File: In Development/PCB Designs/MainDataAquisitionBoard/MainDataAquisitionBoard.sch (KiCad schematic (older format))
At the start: 19 parts, among them J1 Conn_01x08, J10 3v3, J11 TopR, J12 TopL, J13 BottomR, J14 BottomL, J15 RTC, J2 Conn_01x08, J3 GND, J4 1x24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

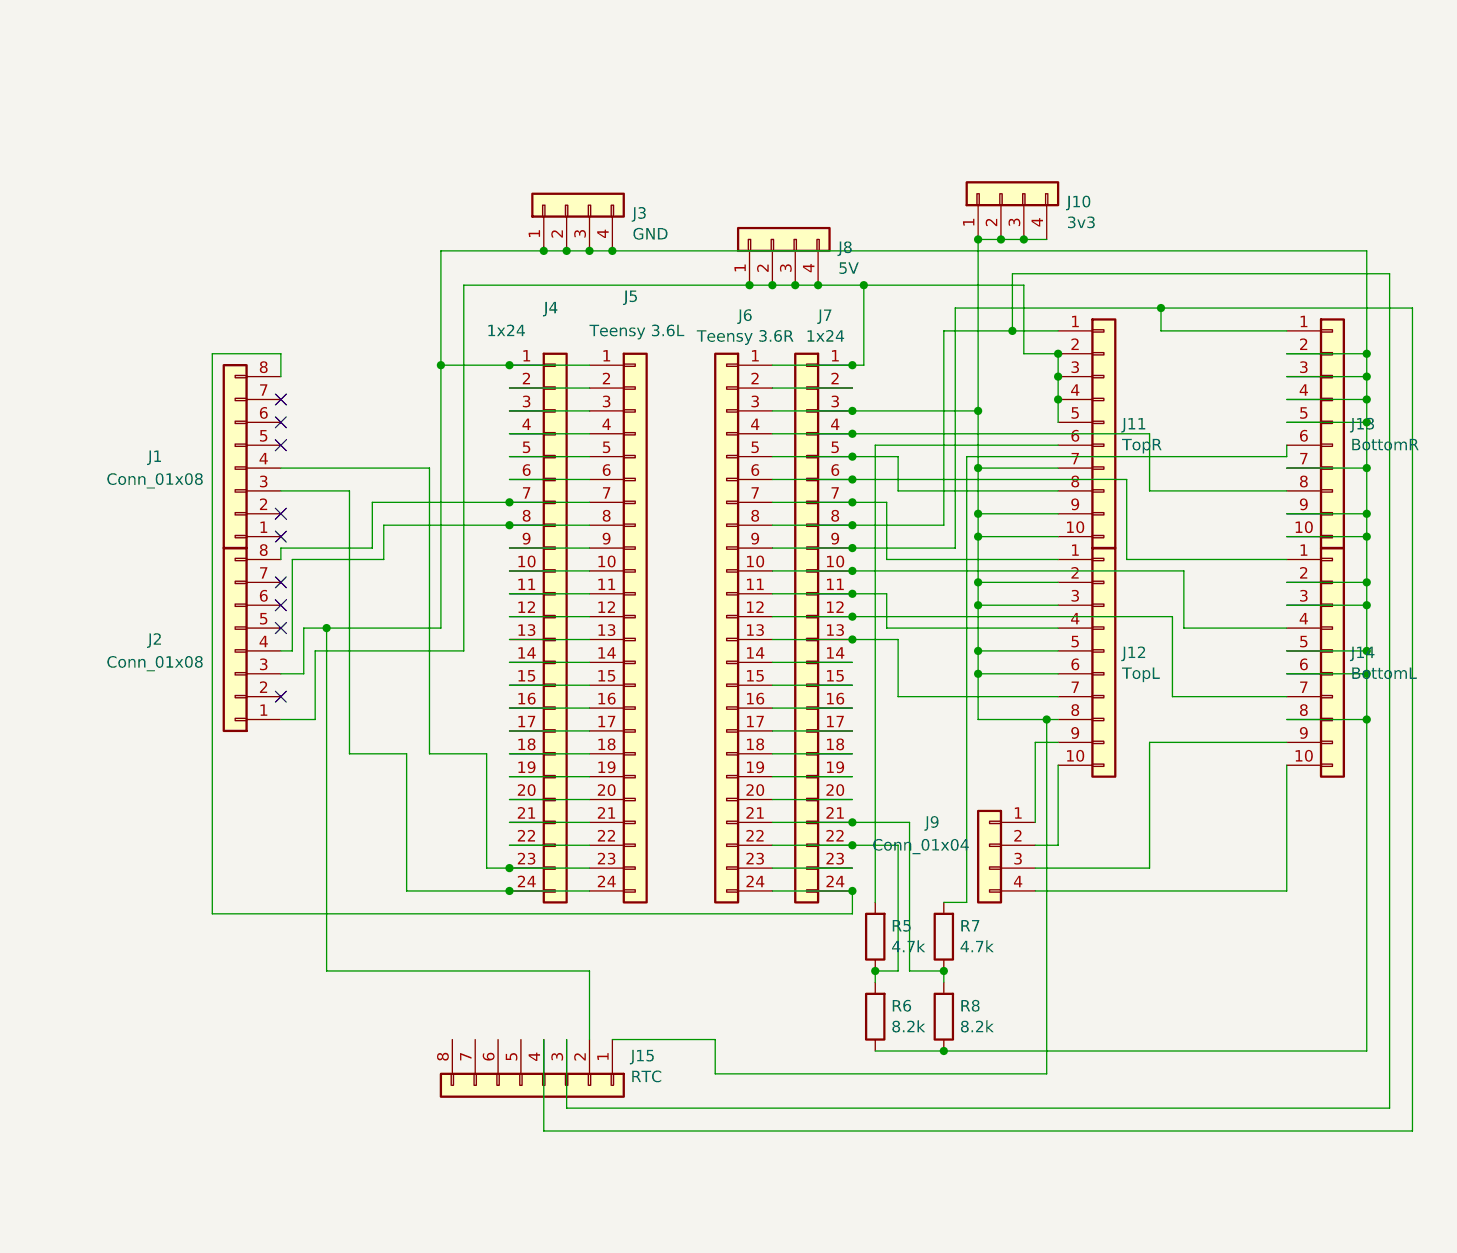
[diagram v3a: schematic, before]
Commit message: Finished Main DAQ PCB and eCVT controller PCB for design review
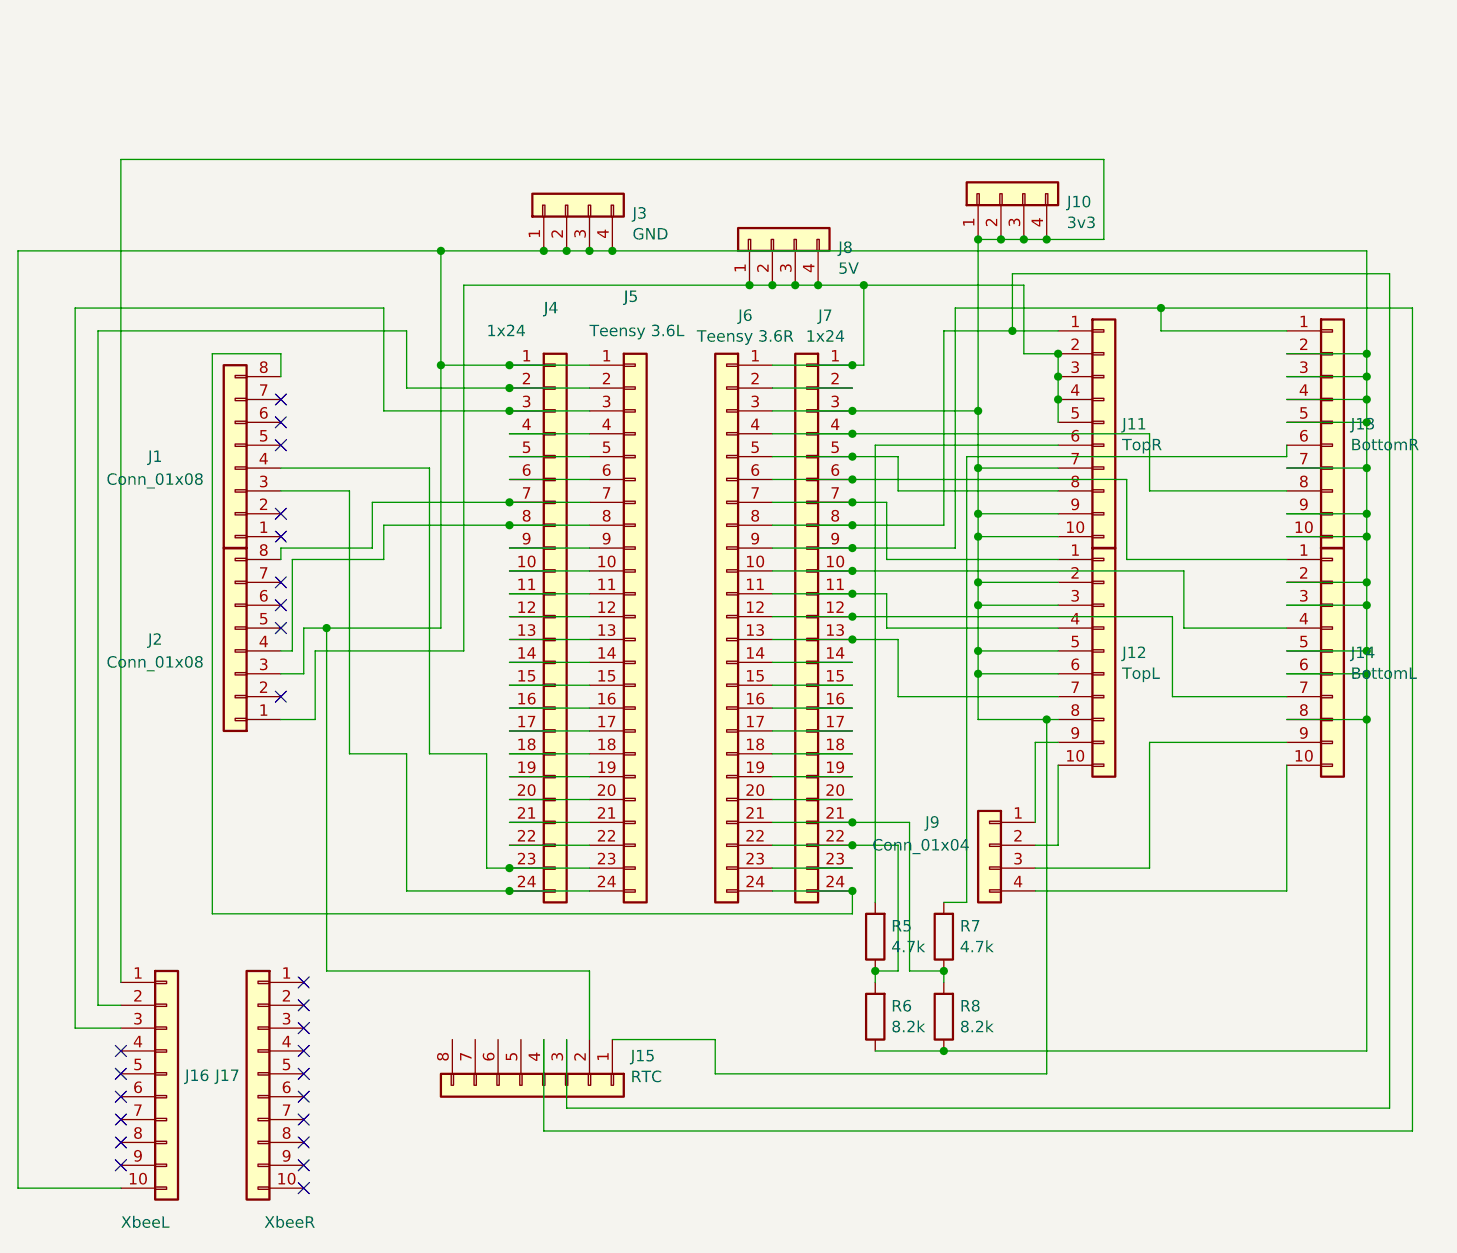
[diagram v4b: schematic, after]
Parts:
- added J16: XbeeL, Connector_PinHeader_2.54mm:PinHeader_1x10_P2.54mm_Vertical, symbol Connector_Generic:Conn_01x10
- added J17: XbeeR, Connector_PinHeader_2.54mm:PinHeader_1x10_P2.54mm_Vertical, symbol Connector_Generic:Conn_01x10
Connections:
- net at J13.10 (Pin_10), J13.2 (Pin_2), J13.3 (Pin_3)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: now also J16.10 (Pin_10)
- net at J4.2 (Pin_2), J5.2 (Pin_2): now also J16.2 (Pin_2)
- net at J4.3 (Pin_3), J5.3 (Pin_3): now also J16.3 (Pin_3)
- net at J10.1 (Pin_1), J10.2 (Pin_2), J10.3 (Pin_3)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: now also J16.1 (Pin_1)
- no-connect marks 9 -> 25
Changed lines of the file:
@@
 	4450 3050 4800 3050
-Wire Wire Line
-	4450 3150 4800 3150
 Wire Wire Line
 	4450 3250 4800 3250
@@
 Wire Wire Line
 	3650 4100 3650 5600
+$Comp
+L Connector_Generic:Conn_01x10 J16
+U 1 1 5E2846AA
+P 2950 6050
+F 0 "J16" H 3030 6042 50  0000 L CNN
+F 1 "XbeeL" H 2750 5400 50  0000 L CNN
+F 2 "Connector_PinHeader_2.54mm:PinHeader_1x10_P2.54mm_Vertical" H 2950 6050 50  0001 C CNN
+F 3 "~" H 2950 6050 50  0001 C CNN
+	1    2950 6050
+	1    0    0    -1
+$EndComp
+NoConn ~ 3550 5650
+NoConn ~ 3550 5750
+NoConn ~ 3550 5850
+NoConn ~ 3550 5950
+NoConn ~ 3550 6050
+NoConn ~ 3550 6150
+NoConn ~ 3550 6250
+NoConn ~ 3550 6350
+NoConn ~ 3550 6450
+NoConn ~ 3550 6550
+NoConn ~ 2750 6450
+NoConn ~ 2750 6350
+NoConn ~ 2750 6250
+NoConn ~ 2750 6150
+NoConn ~ 2750 6050
+NoConn ~ 2750 5950
+Wire Wire Line
+	2750 6550 2300 6550
+Wire Wire Line
+	2300 6550 2300 2450
+Wire Wire Line
+	2300 2450 4150 2450
+Connection ~ 4150 2450
+$Comp
+L Connector_Generic:Conn_01x10 J17
+U 1 1 5E28781E
+P 3350 6050
+F 0 "J17" H 3430 6042 50  0000 L CNN
+F 1 "XbeeR" H 3100 5400 50  0000 L CNN
+F 2 "Connector_PinHeader_2.54mm:PinHeader_1x10_P2.54mm_Vertical" H 3350 6050 50  0001 C CNN
+F 3 "~" H 3350 6050 50  0001 C CNN
+	1    3350 6050
+	-1   0    0    -1
+$EndComp
+Wire Wire Line
+	2750 5650 2750 2050
+Wire Wire Line
+	2750 2050 7050 2050
+Wire Wire Line
+	7050 2050 7050 2400
+Wire Wire Line
+	7050 2400 6800 2400
+Connection ~ 6800 2400
+Wire Wire Line
+	2750 5750 2650 5750
+Wire Wire Line
+	2650 5750 2650 2800
+Wire Wire Line
+	2650 2800 4000 2800
+Wire Wire Line
+	4000 2800 4000 3050
+Wire Wire Line
+	4000 3050 4450 3050
+Connection ~ 4450 3050
+Wire Wire Line
+	2750 5850 2550 5850
+Wire Wire Line
+	2550 5850 2550 2700
+Wire Wire Line
+	2550 2700 3900 2700
+Wire Wire Line
+	3900 2700 3900 3150
+Wire Wire Line
+	3900 3150 4450 3150
+Connection ~ 4450 3150
+Wire Wire Line
+	4450 3150 4800 3150
 $EndSCHEMATC

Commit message: Finished DAQ board and ready for initial production
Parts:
- added J18: Conn_02x03_Counter_Clockwise, Connector_PinHeader_2.54mm:PinHeader_2x03_P2.54mm_Vertical, symbol Connector_Generic:Conn_02x03_Counter_Clockwise
- added J19: Power in, CustomKiCADLibrary:PinHeader_1x02_P5.08mm_Vertical, symbol Connector_Generic:Conn_01x02
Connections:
- net at J13.10 (Pin_10), J13.2 (Pin_2), J13.3 (Pin_3)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: now also J1.1 (Pin_1), J19.2 (Pin_2); no longer J2.3 (Pin_3)
- net at J4.11 (Pin_11), J5.11 (Pin_11): now also J2.3 (Pin_3)
- net at J4.12 (Pin_12), J5.12 (Pin_12): now also J2.1 (Pin_1)
- net at J11.2 (Pin_2), J11.3 (Pin_3), J11.4 (Pin_4)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: now also J18.1 (Pin_1), J19.1 (Pin_1); no longer J2.1 (Pin_1), J6.1 (Pin_1), J7.1 (Pin_1)
- new net: J18.3 (Pin_3), J6.1 (Pin_1), J7.1 (Pin_1)
- no-connect marks 25 -> 28
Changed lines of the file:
@@
 $EndComp
-Wire Wire Line
-	4250 4200 4250 2600
-Wire Wire Line
-	6000 2600 6000 2950
 Wire Wire Line
 	5600 2950 5950 2950
 Connection ~ 5950 2950
 Wire Wire Line
-	5950 2950 6000 2950
-Wire Wire Line
-	3550 4100 3650 4100
-Wire Wire Line
 	4150 2950 4450 2950
 Connection ~ 4450 2950
@@
 Connection ~ 4450 3550
 Wire Wire Line
-	4100 4650 4350 4650
-Wire Wire Line
 	4350 4650 4350 5150
 Wire Wire Line
@@
 	4450 5150 4800 5150
 Wire Wire Line
-	3750 4650 4000 4650
-Wire Wire Line
-	4000 4650 4000 5250
-Wire Wire Line
 	4000 5250 4450 5250
 Connection ~ 4450 5250
-Connection ~ 3650 4100
-Wire Wire Line
-	3650 4100 4150 4100
-Wire Wire Line
-	4150 2950 4150 4100
-Wire Wire Line
-	6000 2600 6700 2600
 Wire Wire Line
 	6700 2600 6700 2900
 Wire Wire Line
 	6700 2900 6850 2900
-Connection ~ 6000 2600
 Wire Wire Line
 	6850 2900 6850 3000
@@
 Wire Wire Line
 	8200 2900 7850 2900
-Connection ~ 4150 2950
 Wire Wire Line
 	8200 4500 7850 4500
@@
 $EndComp
 Wire Wire Line
-	4900 2450 8200 2450
-Wire Wire Line
 	4600 2450 4700 2450
 Connection ~ 4600 2450
@@
 Wire Wire Line
 	4800 2450 4900 2450
-Wire Wire Line
-	5800 2600 6000 2600
 $Comp
 L Connector_Generic:Conn_01x04 J8
@@
 $EndComp
 Wire Wire Line
-	4250 2600 5500 2600
-Wire Wire Line
 	5500 2600 5600 2600
-Connection ~ 5500 2600
 Connection ~ 5800 2600
 Connection ~ 5600 2600
@@
 	3750 3500 3450 3500
 Wire Wire Line
-	4250 4200 3600 4200
-Wire Wire Line
-	3600 4200 3600 4500
-Wire Wire Line
-	3600 4500 3450 4500
-Wire Wire Line
-	3550 4100 3550 4300
-Wire Wire Line
-	3550 4300 3450 4300
-Wire Wire Line
 	3500 3800 3500 4200
 Wire Wire Line
 	3500 4200 3450 4200
 Wire Wire Line
-	3500 3800 3900 3800
-Wire Wire Line
 	3450 3750 3450 3800
 Wire Wire Line
@@
 Wire Wire Line
 	3450 3750 3850 3750
-NoConn ~ 3450 3700
 Wire Wire Line
 	6050 3300 6050 5300
@@
 	4600 6300 4600 5900
 Connection ~ 7300 2700
-Wire Wire Line
-	4100 3400 4100 4650
-Wire Wire Line
-	3750 3500 3750 4650
-Wire Wire Line
-	3650 4100 3650 5600
 $Comp
 L Connector_Generic:Conn_01x10 J16
@@
 Wire Wire Line
 	4450 3150 4800 3150
+$Comp
+L Connector_Generic:Conn_02x03_Counter_Clockwise J18
+U 1 1 5E28BDCC
+P 6350 1800
+F 0 "J18" H 6400 2117 50  0000 C CNN
+F 1 "Conn_02x03_Counter_Clockwise" H 6400 2026 50  0000 C CNN
+F 2 "Connector_PinHeader_2.54mm:PinHeader_2x03_P2.54mm_Vertical" H 6350 1800 50  0001 C CNN
+F 3 "~" H 6350 1800 50  0001 C CNN
+	1    6350 1800
+	1    0    0    -1
+$EndComp
+Wire Wire Line
+	5800 2600 5900 2600
+Wire Wire Line
+	5900 2600 5900 1700
+Wire Wire Line
+	5900 1700 6150 1700
+Connection ~ 5900 2600
+Wire Wire Line
+	5900 2600 6700 2600
+Wire Wire Line
+	6150 1900 6150 2950
+Wire Wire Line
+	5950 2950 6150 2950
+NoConn ~ 6150 1800
+NoConn ~ 6650 1700
+NoConn ~ 6650 1800
+NoConn ~ 6650 1900
+Connection ~ 4150 2950
+Wire Wire Line
+	3500 3800 3900 3800
+Wire Wire Line
+	3650 4100 3650 5600
+Wire Wire Line
+	3750 3500 3750 4650
+Wire Wire Line
+	4100 3400 4100 4650
+Wire Wire Line
+	4150 2950 4150 3700
+Wire Wire Line
+	3650 4100 4150 4100
+Wire Wire Line
+	4000 4650 4000 5250
+Wire Wire Line
+	3750 4650 4000 4650
+Wire Wire Line
+	4100 4650 4350 4650
+Wire Wire Line
+	3450 3700 4150 3700
+Connection ~ 4150 3700
+Wire Wire Line
+	4150 3700 4150 4100
+Wire Wire Line
+	3450 4300 4300 4300
+Wire Wire Line
+	4300 4300 4300 3950
+Wire Wire Line
+	4300 3950 4450 3950
+Connection ~ 4450 3950
+Wire Wire Line
+	3450 4500 4350 4500
+Wire Wire Line
+	4350 4500 4350 4050
+Wire Wire Line
+	4350 4050 4450 4050
+Connection ~ 4450 4050
+$Comp
+L Connector_Generic:Conn_01x02 J19
+U 1 1 5E3C057F
+P 5050 1650
+F 0 "J19" V 5014 1462 50  0000 R CNN
+F 1 "Power in" V 4923 1462 50  0000 R CNN
+F 2 "CustomKiCADLibrary:PinHeader_1x02_P5.08mm_Vertical" H 5050 1650 50  0001 C CNN
+F 3 "~" H 5050 1650 50  0001 C CNN
+	1    5050 1650
+	0    -1   -1   0
+$EndComp
+Wire Wire Line
+	5050 1850 5050 2600
+Wire Wire Line
+	5050 2600 5500 2600
+Connection ~ 5500 2600
+Wire Wire Line
+	5150 1850 5150 2450
+Wire Wire Line
+	4900 2450 5150 2450
+Connection ~ 5150 2450
+Wire Wire Line
+	5150 2450 8200 2450
 $EndSCHEMATC
